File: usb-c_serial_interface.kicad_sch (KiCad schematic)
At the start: 37 parts, among them J1 12401598E4#2A, J2 PH1-07-UA, J3 PH1-06-UA, J6 USB-C Serial-Footprint (16U2), J8 USB-C Serial-Footprint (16U2), Q2 2N7000BU, U1 ATMEGA16U2, Y1 FTX16.000M12SM3S-30/30

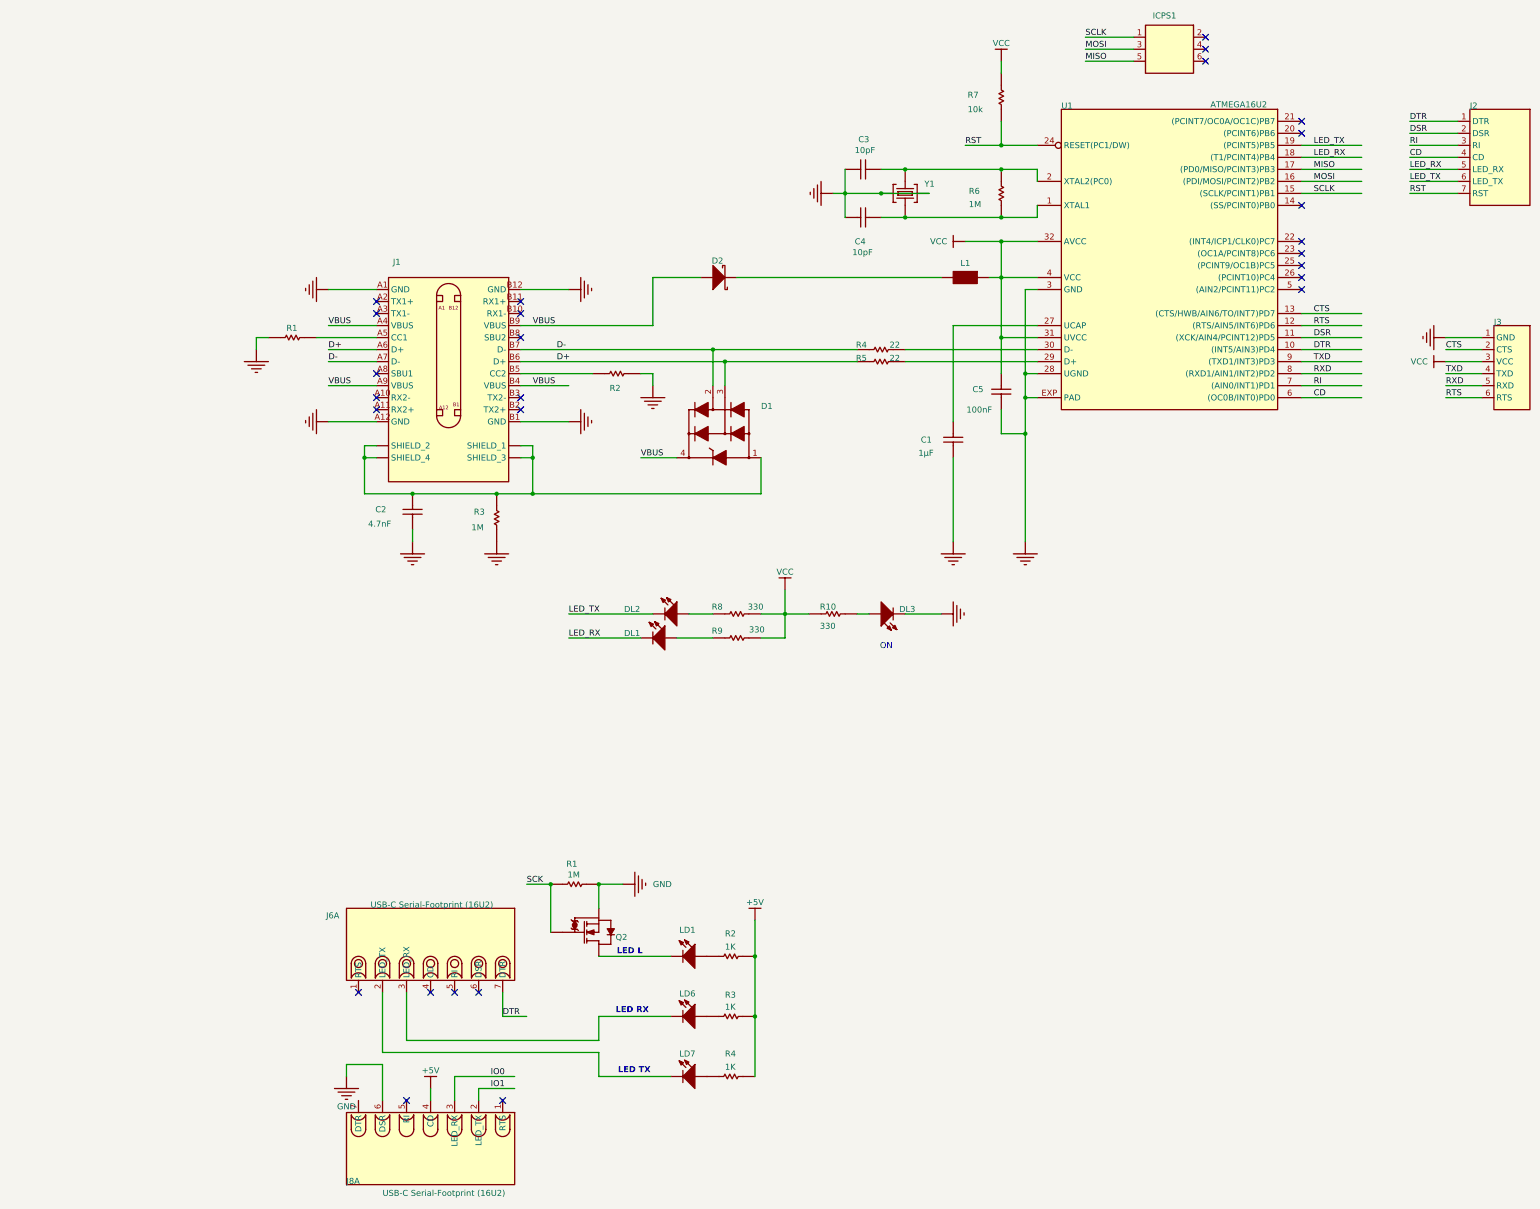
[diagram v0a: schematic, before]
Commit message: started cleanup, need to do sheet labels
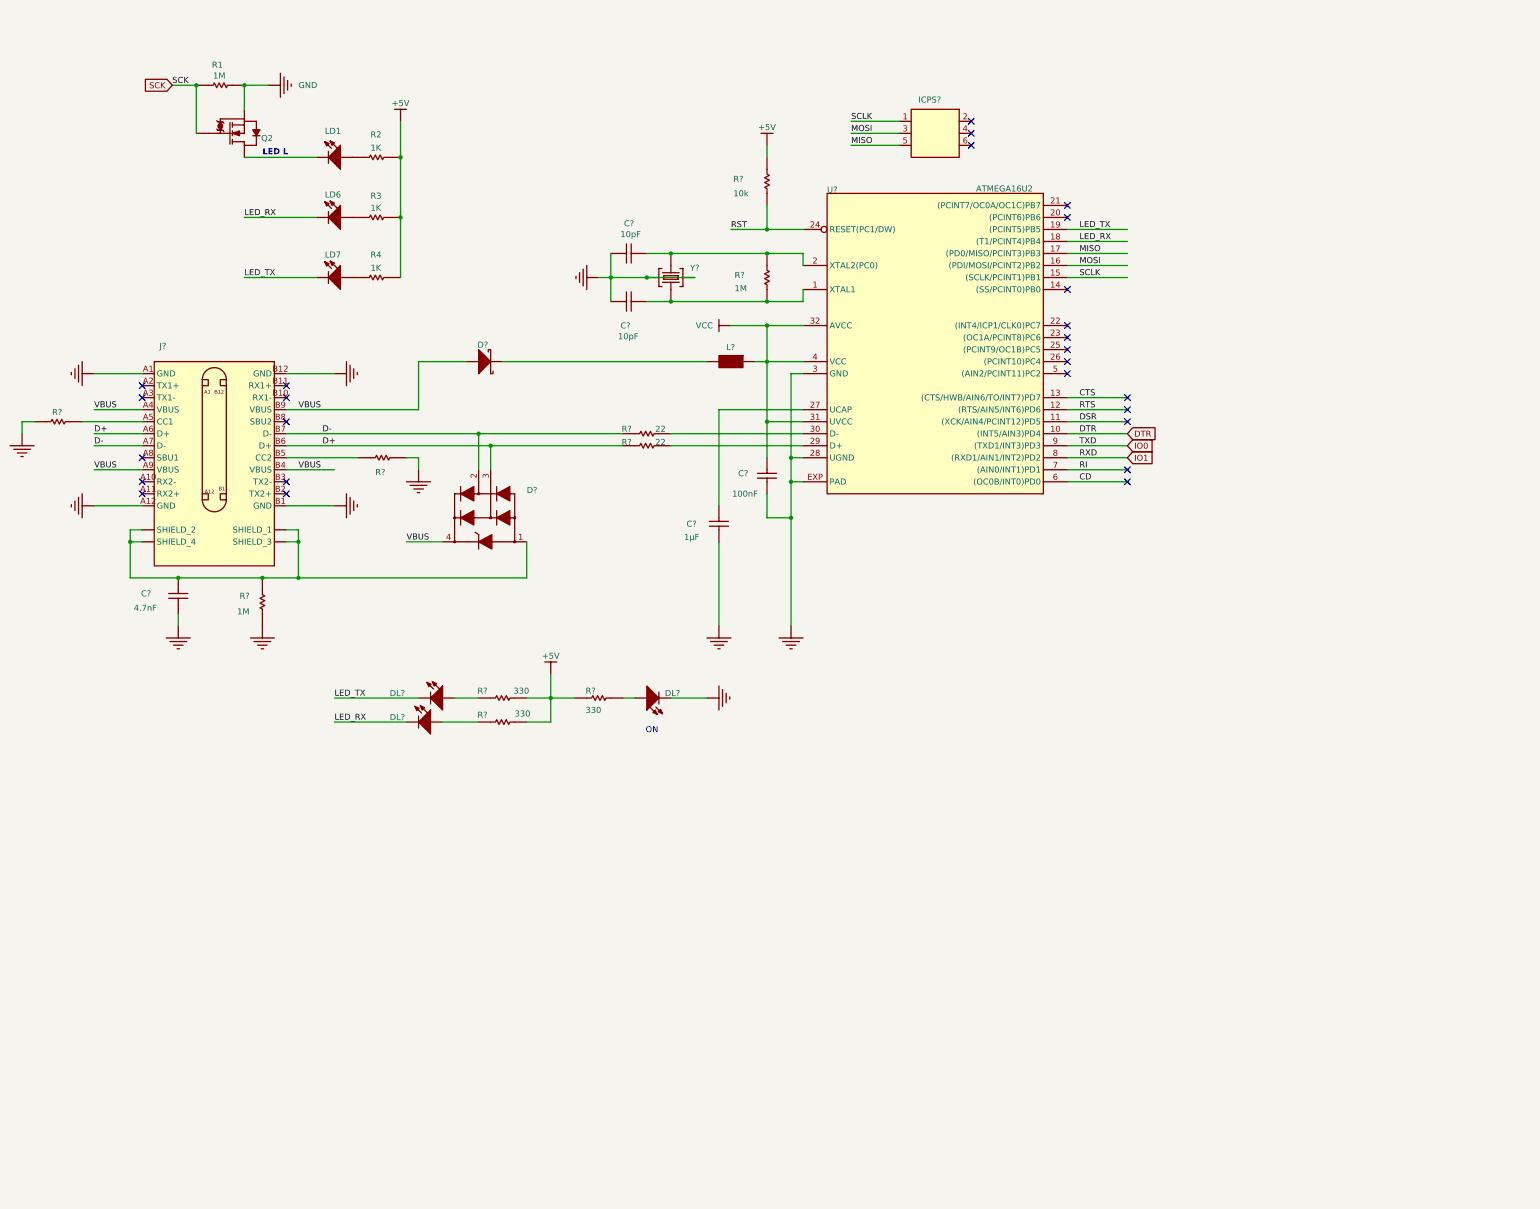
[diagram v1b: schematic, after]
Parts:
- removed J2: PH1-07-UA, CONN STRIP 2.54 PIN HEADER DIP 180° 1x 7 PIN GOLD FLASH castelleted, symbol USB-C_Serial_16U2-altium-import:0_PH1-07-UA
- removed J3: PH1-06-UA, CONN STRP 2.54 PIN HEADER DIP 180° 1x X PIN GOLD FLASH, symbol USB-C_Serial_16U2-altium-import:0_PH1-06-UA
- removed J6: USB-C Serial-Footprint (16U2), USB-C Serial-Footprint (16U2), symbol Arduino_Uno_Kit-altium-import:1_USB-C Serial CARRIER
- removed J8: USB-C Serial-Footprint (16U2), USB-C Serial-Footprint (16U2), symbol Arduino_Uno_Kit-altium-import:3_USB-C Serial CARRIER
- renumbered C4 to C?, C1 to C?, C2 to C?, C3 to C?, C5 to C?, D2 to D?, D1 to D?, DL1 to DL?, DL2 to DL?, DL3 to DL?, ICPS1 to ICPS?, J1 to J?, L1 to L?, R8 to R?, R2 to R?, R7 to R?, R9 to R?, R5 to R?, R1 to R?, R10 to R?, R4 to R?, R6 to R?, R3 to R?, U1 to U?, Y1 to Y?
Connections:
- net RXD is gone; now on net IO1: U?.8 ((RXD1/AIN1/INT2)PD2)
- net TXD is gone; now on net IO0: U?.9 ((TXD1/INT3)PD3)
- net +5V: now also R?.1, R?.2, R?.2, R?.2
- net LED_RX: now also LD6.C
- net LED_TX: now also LD7.C
- net VCC: no longer R?.1, R?.2, R?.2, R?.2
- no-connect marks 27 -> 26
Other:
- note removed: "LED RX"
- note removed: "LED TX"
- moved on the sheet: C?, D?, DL?, ICPS?, J?, L?, LD1, LD6, LD7, Q2, R1, R2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
